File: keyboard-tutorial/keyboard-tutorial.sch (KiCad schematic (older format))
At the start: 13 parts

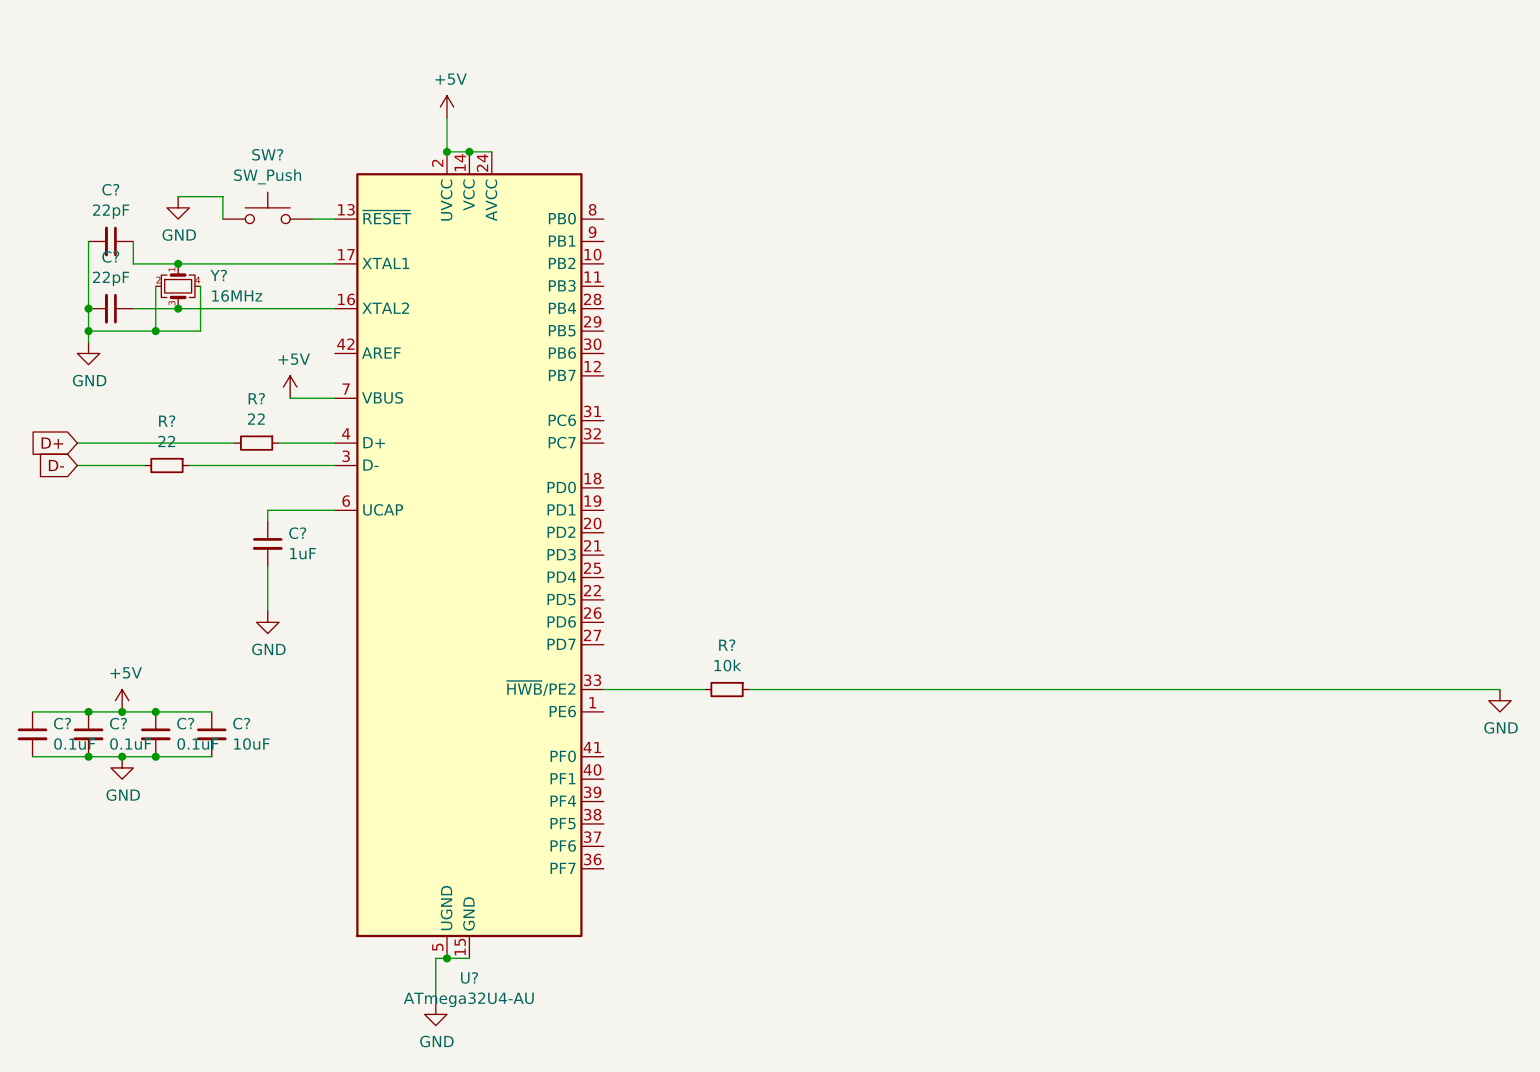
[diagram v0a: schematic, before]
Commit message: Added USB bus and switch matrix
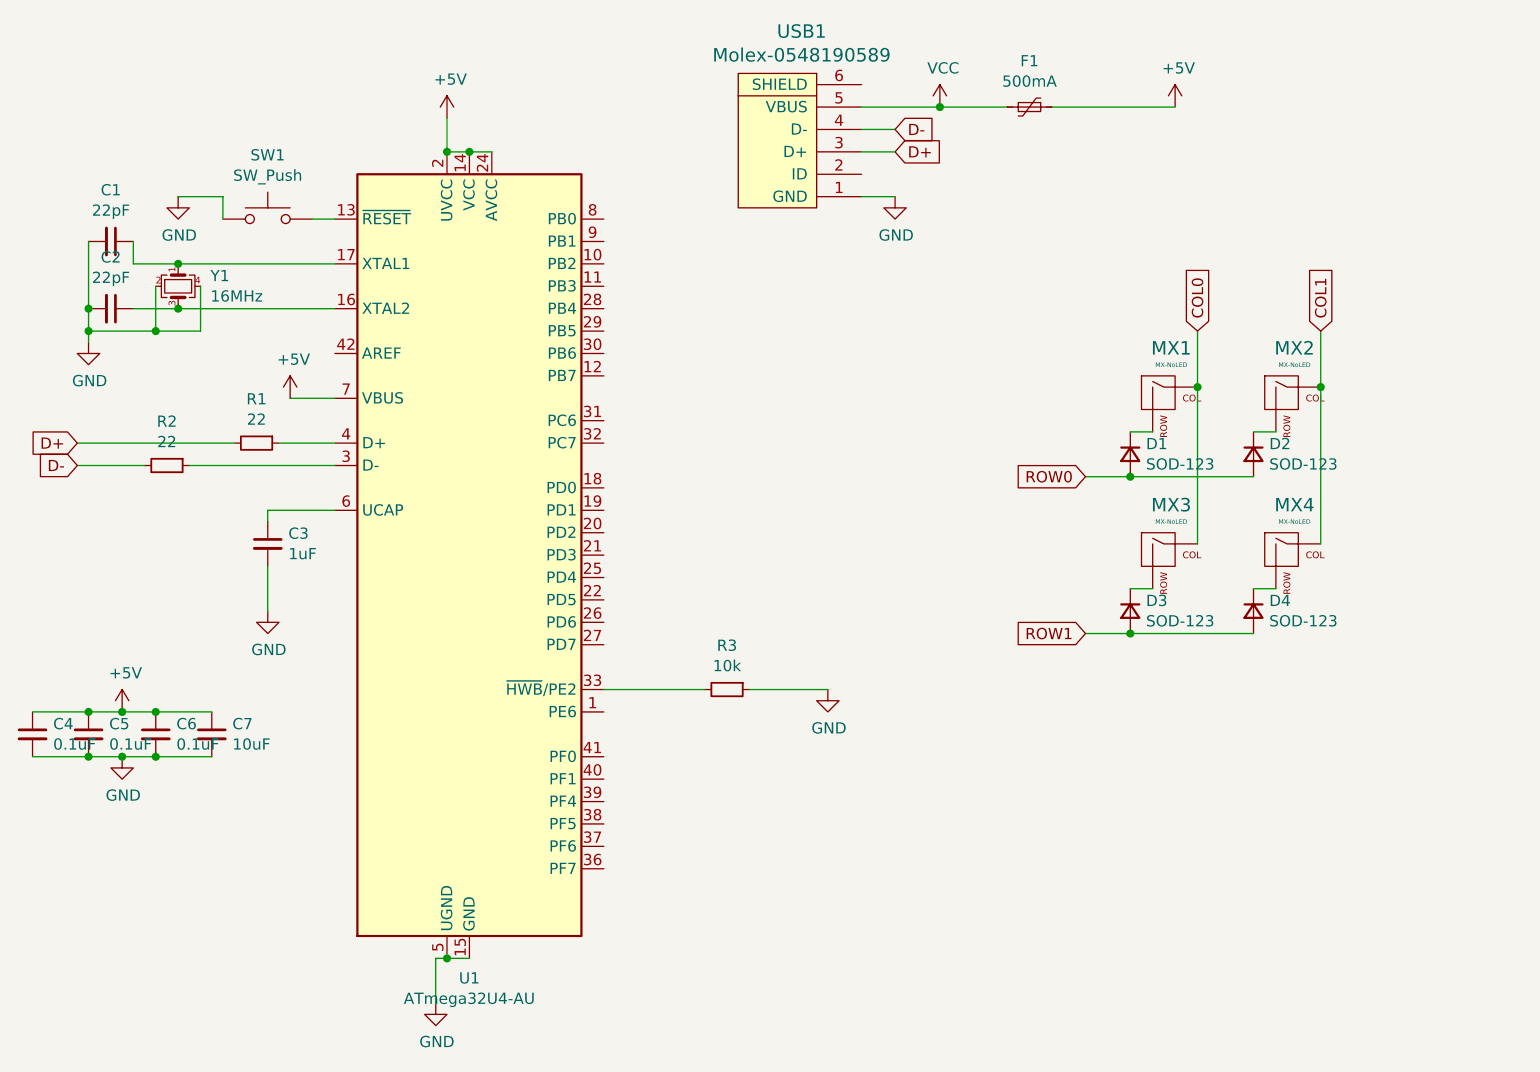
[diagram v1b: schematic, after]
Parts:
- added D1, D2, D3, D4: SOD-123, symbol Device:D_Small
- added F1: 500mA, symbol Device:Polyfuse_Small
- added MX1, MX2, MX3, MX4: MX-NoLED, symbol MX_Alps_Hybrid:MX-NoLED
- added USB1: Molex-0548190589, symbol random-keyboard-parts:Molex-0548190589
- gave numbers to parts that had none: 13
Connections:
- net +5V: now also F1.1
- net D+: now also USB1.3 (D+)
- net D-: now also USB1.4 (D-)
- net GND: now also USB1.1 (GND)
- new net: D1.1 (K), MX1.2 (ROW)
- new net: D2.1 (K), MX2.2 (ROW)
- new net: D3.1 (K), MX3.2 (ROW)
- new net: D4.1 (K), MX4.2 (ROW)
- new net COL0: MX1.1 (COL), MX3.1 (COL)
- new net COL1: MX2.1 (COL), MX4.1 (COL)
- new net ROW0: D1.2 (A), D2.2 (A)
- new net ROW1: D3.2 (A), D4.2 (A)
- new net VCC: F1.2, USB1.5 (VBUS)

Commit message: Assigned PCB footprints to schematic
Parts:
- C1, C2, C3, C4, C5, C6, C7: footprint (none) -> Capacitor_SMD:C_0805_2012Metric
- D1, D2, D3, D4: footprint (none) -> Diode_SMD:D_SOD-123
- F1: footprint (none) -> Fuse:Fuse_1206_3216Metric
- MX1, MX2, MX3, MX4: footprint (none) -> MX_Alps_Hybrid:MX-1U-NoLED
- R1, R2, R3: footprint (none) -> Resistor_SMD:R_0805_2012Metric
- SW1: footprint (none) -> random-keyboard-parts:SKQG-1155865
- USB1: footprint (none) -> random-keyboard-parts:Molex-0548190589
- Y1: footprint (none) -> Crystal:Crystal_SMD_3225-4Pin_3.2x2.5mm
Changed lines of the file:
@@
 F 0 "R3" V 4354 3800 50  0000 C CNN
 F 1 "10k" V 4445 3800 50  0000 C CNN
-F 2 "" H 4550 3800 50  0001 C CNN
+F 2 "Resistor_SMD:R_0805_2012Metric" H 4550 3800 50  0001 C CNN
 F 3 "~" H 4550 3800 50  0001 C CNN
 	1    4550 3800
@@
 F 0 "R1" V 2254 2700 50  0000 C CNN
 F 1 "22" V 2345 2700 50  0000 C CNN
-F 2 "" H 2450 2700 50  0001 C CNN
+F 2 "Resistor_SMD:R_0805_2012Metric" H 2450 2700 50  0001 C CNN
 F 3 "~" H 2450 2700 50  0001 C CNN
 	1    2450 2700
@@
 F 0 "R2" V 1854 2800 50  0000 C CNN
 F 1 "22" V 1945 2800 50  0000 C CNN
-F 2 "" H 2050 2800 50  0001 C CNN
+F 2 "Resistor_SMD:R_0805_2012Metric" H 2050 2800 50  0001 C CNN
 F 3 "~" H 2050 2800 50  0001 C CNN
 	1    2050 2800
@@
 F 0 "C3" H 2592 3196 50  0000 L CNN
 F 1 "1uF" H 2592 3105 50  0000 L CNN
-F 2 "" H 2500 3150 50  0001 C CNN
+F 2 "Capacitor_SMD:C_0805_2012Metric" H 2500 3150 50  0001 C CNN
 F 3 "~" H 2500 3150 50  0001 C CNN
 	1    2500 3150
@@
 F 0 "C4" H 1542 4046 50  0000 L CNN
 F 1 "0.1uF" H 1542 3955 50  0000 L CNN
-F 2 "" H 1450 4000 50  0001 C CNN
+F 2 "Capacitor_SMD:C_0805_2012Metric" H 1450 4000 50  0001 C CNN
 F 3 "~" H 1450 4000 50  0001 C CNN
 	1    1450 4000
@@
 F 0 "C5" H 1792 4046 50  0000 L CNN
 F 1 "0.1uF" H 1792 3955 50  0000 L CNN
-F 2 "" H 1700 4000 50  0001 C CNN
+F 2 "Capacitor_SMD:C_0805_2012Metric" H 1700 4000 50  0001 C CNN
 F 3 "~" H 1700 4000 50  0001 C CNN
 	1    1700 4000
@@
 F 0 "C6" H 2092 4046 50  0000 L CNN
 F 1 "0.1uF" H 2092 3955 50  0000 L CNN
-F 2 "" H 2000 4000 50  0001 C CNN
+F 2 "Capacitor_SMD:C_0805_2012Metric" H 2000 4000 50  0001 C CNN
 F 3 "~" H 2000 4000 50  0001 C CNN
 	1    2000 4000
@@
 F 0 "C7" H 2342 4046 50  0000 L CNN
 F 1 "10uF" H 2342 3955 50  0000 L CNN
-F 2 "" H 2250 4000 50  0001 C CNN
+F 2 "Capacitor_SMD:C_0805_2012Metric" H 2250 4000 50  0001 C CNN
 F 3 "~" H 2250 4000 50  0001 C CNN
 	1    2250 4000
@@
 F 0 "Y1" V 2054 2144 50  0000 L CNN
 F 1 "16MHz" V 2145 2144 50  0000 L CNN
-F 2 "" H 2100 2000 50  0001 C CNN
+F 2 "Crystal:Crystal_SMD_3225-4Pin_3.2x2.5mm" H 2100 2000 50  0001 C CNN
 F 3 "~" H 2100 2000 50  0001 C CNN
 	1    2100 2000
@@
 F 0 "C1" V 1571 1800 50  0000 C CNN
 F 1 "22pF" V 1662 1800 50  0000 C CNN
-F 2 "" H 1800 1800 50  0001 C CNN
+F 2 "Capacitor_SMD:C_0805_2012Metric" H 1800 1800 50  0001 C CNN
 F 3 "~" H 1800 1800 50  0001 C CNN
 	1    1800 1800
@@
 F 0 "C2" V 1571 2100 50  0000 C CNN
 F 1 "22pF" V 1662 2100 50  0000 C CNN
-F 2 "" H 1800 2100 50  0001 C CNN
+F 2 "Capacitor_SMD:C_0805_2012Metric" H 1800 2100 50  0001 C CNN
 F 3 "~" H 1800 2100 50  0001 C CNN
 	1    1800 2100
@@
 F 0 "SW1" H 2500 1985 50  0000 C CNN
 F 1 "SW_Push" H 2500 1894 50  0000 C CNN
-F 2 "" H 2500 1900 50  0001 C CNN
+F 2 "random-keyboard-parts:SKQG-1155865" H 2500 1900 50  0001 C CNN
 F 3 "~" H 2500 1900 50  0001 C CNN
 	1    2500 1700
@@
 F 0 "USB1" V 5387 1367 60  0000 C CNN
 F 1 "Molex-0548190589" V 5281 1367 60  0000 C CNN
-F 2 "" H 4850 1400 60  0001 C CNN
+F 2 "random-keyboard-parts:Molex-0548190589" H 4850 1400 60  0001 C CNN
 F 3 "" H 4850 1400 60  0001 C CNN
 	1    4850 1400
@@
 F 0 "F1" V 5695 1200 50  0000 C CNN
 F 1 "500mA" V 5786 1200 50  0000 C CNN
-F 2 "" H 5950 1000 50  0001 L CNN
+F 2 "Fuse:Fuse_1206_3216Metric" H 5950 1000 50  0001 L CNN
 F 3 "~" H 5900 1200 50  0001 C CNN
 	1    5900 1200
@@
 F 0 "MX1" H 6533 2723 60  0000 C CNN
 F 1 "MX-NoLED" H 6533 2649 20  0000 C CNN
-F 2 "" H 5875 2475 60  0001 C CNN
+F 2 "MX_Alps_Hybrid:MX-1U-NoLED" H 5875 2475 60  0001 C CNN
 F 3 "" H 5875 2475 60  0001 C CNN
 	1    6500 2500
@@
 F 0 "MX2" H 7083 2723 60  0000 C CNN
 F 1 "MX-NoLED" H 7083 2649 20  0000 C CNN
-F 2 "" H 6425 2475 60  0001 C CNN
+F 2 "MX_Alps_Hybrid:MX-1U-NoLED" H 6425 2475 60  0001 C CNN
 F 3 "" H 6425 2475 60  0001 C CNN
 	1    7050 2500
@@
 F 0 "MX3" H 6533 3423 60  0000 C CNN
 F 1 "MX-NoLED" H 6533 3349 20  0000 C CNN
-F 2 "" H 5875 3175 60  0001 C CNN
+F 2 "MX_Alps_Hybrid:MX-1U-NoLED" H 5875 3175 60  0001 C CNN
 F 3 "" H 5875 3175 60  0001 C CNN
 	1    6500 3200
@@
 F 0 "MX4" H 7083 3423 60  0000 C CNN
 F 1 "MX-NoLED" H 7083 3349 20  0000 C CNN
-F 2 "" H 6425 3175 60  0001 C CNN
+F 2 "MX_Alps_Hybrid:MX-1U-NoLED" H 6425 3175 60  0001 C CNN
 F 3 "" H 6425 3175 60  0001 C CNN
 	1    7050 3200
@@
 F 0 "D1" V 6304 2820 50  0000 L CNN
 F 1 "SOD-123" V 6395 2820 50  0000 L CNN
-F 2 "" V 6350 2750 50  0001 C CNN
+F 2 "Diode_SMD:D_SOD-123" V 6350 2750 50  0001 C CNN
 F 3 "~" V 6350 2750 50  0001 C CNN
 	1    6350 2750
@@
 F 0 "D2" V 6854 2820 50  0000 L CNN
 F 1 "SOD-123" V 6945 2820 50  0000 L CNN
-F 2 "" V 6900 2750 50  0001 C CNN
+F 2 "Diode_SMD:D_SOD-123" V 6900 2750 50  0001 C CNN
 F 3 "~" V 6900 2750 50  0001 C CNN
 	1    6900 2750
@@
 F 0 "D4" V 6854 3520 50  0000 L CNN
 F 1 "SOD-123" V 6945 3520 50  0000 L CNN
-F 2 "" V 6900 3450 50  0001 C CNN
+F 2 "Diode_SMD:D_SOD-123" V 6900 3450 50  0001 C CNN
 F 3 "~" V 6900 3450 50  0001 C CNN
 	1    6900 3450
@@
 F 0 "D3" V 6304 3520 50  0000 L CNN
 F 1 "SOD-123" V 6395 3520 50  0000 L CNN
-F 2 "" V 6350 3450 50  0001 C CNN
+F 2 "Diode_SMD:D_SOD-123" V 6350 3450 50  0001 C CNN
 F 3 "~" V 6350 3450 50  0001 C CNN
 	1    6350 3450
